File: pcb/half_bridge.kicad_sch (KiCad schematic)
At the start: 14 parts, among them Q1 IKW40N120H3, Q2 IKW40N120H3, U1 UCC21550BDWK

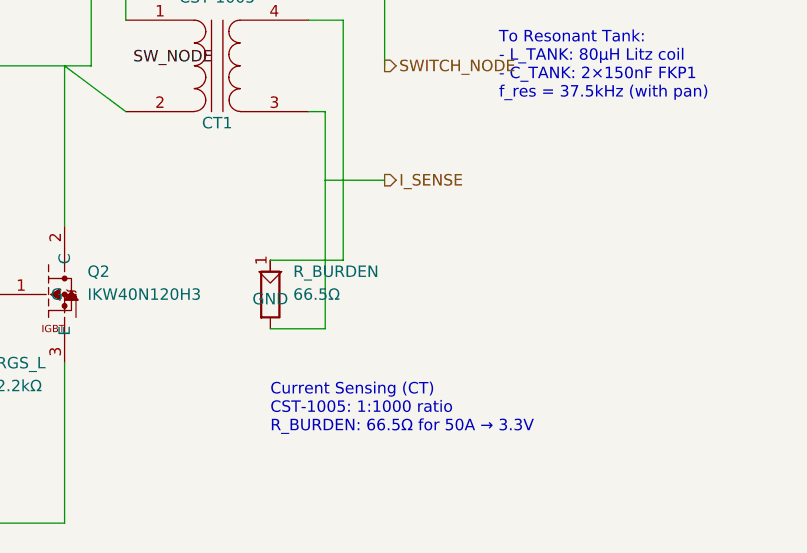
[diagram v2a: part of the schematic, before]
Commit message: fix: correct SN74HC4075 pin map in components.ato; add missing CT filter cap
- elec/src/components.ato: SN74HC4075's gate 1/gate 3 pin numbers were
  wrong (documented as a known bug in a prior session but never fixed at
  the source). Corrected to the real datasheet pinout. All modules.ato
  wiring refers to this part by signal name, not raw pin number, so the
  fix required no other changes.
- pcb/half_bridge.kicad_sch: added C_FILTER (100nF), the CT sense HF filter
  cap that elec/src/modules.ato's CurrentSensing module specifies but that
  was never drawn in either the old or new schematic location.

Co-Authored-By: Claude Sonnet 5 <noreply@anthropic.com>
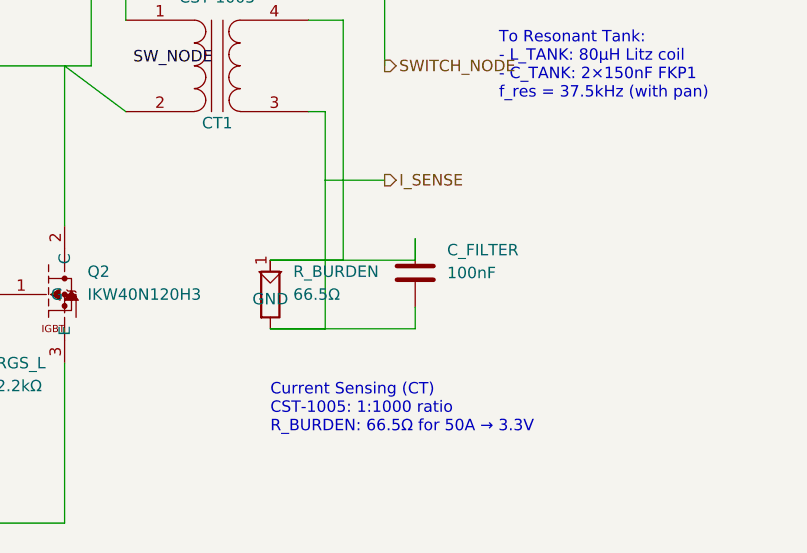
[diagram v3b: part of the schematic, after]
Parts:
- added C_FILTER: 100nF, Capacitor_SMD:C_0603_1608Metric, symbol Device:C
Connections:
- net GND: now also C_FILTER.1
- net I_SENSE: now also C_FILTER.2
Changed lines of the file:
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@@
   )
+  (symbol
+    (lib_id "Device:C")
+    (at 232.0 150.0 0)
+    (unit 1)
+    (exclude_from_sim no)
+    (in_bom yes)
+    (on_board yes)
+    (dnp no)
+    (property "Reference" "C_FILTER" (at 235.54 147.46 0) (effects (font (size 1.27 1.27)) (justify left)))
+    (property "Value" "100nF" (at 235.54 150.0 0) (effects (font (size 1.27 1.27)) (justify left)))
+    (property "Footprint" "Capacitor_SMD:C_0603_1608Metric" (at 233.7652 153.81 0) (effects (font (size 1.27 1.27)) hide))
+    (property "MPN" "GRM1885C1H104JA01D" (at 232.0 150.0 0) (effects (font (size 1.27 1.27)) hide))
+    (property "Description" "CT sense HF noise filter, per elec/src/modules.ato CurrentSensing.c_filter" (at 232.0 150.0 0) (effects (font (size 1.27 1.27)) hide))
+    (pin "1" (uuid "cfilter-pin1-uuid"))
+    (pin "2" (uuid "cfilter-pin2-uuid"))
+  )
+  (wire (pts (xy 215.9 156.21) (xy 232.0 156.21)) (stroke (width 0) (type default)) (uuid "wire-cfilter-001"))
+  (wire (pts (xy 232.0 156.21) (xy 232.0 153.81)) (stroke (width 0) (type default)) (uuid "wire-cfilter-002"))
+  (wire (pts (xy 232.0 146.19) (xy 232.0 148.59)) (stroke (width 0) (type default)) (uuid "wire-cfilter-003"))
+  (wire (pts (xy 232.0 148.59) (xy 215.9 148.59)) (stroke (width 0) (type default)) (uuid "wire-cfilter-004"))
   (symbol
     (lib_id "power:GND")

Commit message: feat: hand-build custom footprints from real datasheets (relay, CT, DC-DC), fix stale footprint references
Draws the three custom footprints that were previously deferred as
"mechanical CAD work" -- .kicad_mod is the same S-expression text format
as .kicad_sch, and all three parts have public datasheets with real
mechanical dimensions:

- pcb/libs/temper.pretty/Relay_SPST_Omron-G4A-E.kicad_mod: Omron G4A-1A-E
  relay. Coil pins (6.35mm pitch) and #250 Faston contact terminals sourced
  from the official Omron datasheet. Confirmed via the datasheet's own
  Model Number Legend text (not an inferred drawing detail) that the
  contacts have zero PCB copper connection on this variant -- modeled as
  placeholder SMD pads for symbol/footprint pin-count parity only.
  Mounting-hole positions are flagged for a human visual cross-check
  against the datasheet before fabrication.
- pcb/libs/temper.pretty/CST-1005.kicad_mod: Triad Magnetics CST-1005
  current sense transformer. Secondary pin pitch, primary window diameter,
  and pin diameter are all high-confidence, unambiguous datasheet table
  values.
- pcb/libs/temper.pretty/Converter_DCDC_RECOM_RP-S.kicad_mod: RECOM RP-1505S
  isolated DC-DC. Best-sourced of the three -- clean table data including
  the real SIP7 populated-pin pattern (2 of 7 positions genuinely absent on
  the single-output variant), cross-checked via two independently-labeled
  span dimensions in the datasheet. Replaces a Footprint reference that
  pointed at a library entry that didn't exist in any installed KiCad
  library.

All three footprints' pad numbers were remapped to match the already-placed
KiCad symbols' generic pin numbering (not the datasheets' own silkscreen
pin numbers), with the real-part mapping documented in each file's descr
field, after catching that a naive 1:1 pad-number assumption would have
mismatched the symbols.

Also: elec/src/footprints.ato's separate (not yet build-wired) generative
CST1005_Footprint module had an unsourced p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
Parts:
- CT1: footprint CST1005_Footprint -> temper:CST-1005
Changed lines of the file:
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@@
     (property "Reference" "CT1" (at 210.0 133.35 0) (effects (font (size 1.27 1.27))))
     (property "Value" "CST-1005" (at 210.0 119.38 0) (effects (font (size 1.27 1.27))))
-    (property "Footprint" "CST1005_Footprint" (at 210.0 127.0 0) (effects (font (size 1.27 1.27)) hide))
+    (property "Footprint" "temper:CST-1005" (at 210.0 127.0 0) (effects (font (size 1.27 1.27)) hide))
     (property "MPN" "CST-1005" (at 210.0 127.0 0) (effects (font (size 1.27 1.27)) hide))
     (property "Description" "Current transformer 1:1000, primary threaded in series with SWITCH_NODE/tank current, secondary across R_BURDEN" (at 210.0 127.0 0) (effects (font (size 1.27 1.27)) hide))
